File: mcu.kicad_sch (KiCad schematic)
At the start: 43 parts, among them J5 Conn_01x04_Socket, SW1 SW_Push, SW2 SW_Push, U2 ESP32-S3-WROOM-1, U3 SN74AXC4T245PWR, Y1 32.768kHz

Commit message: Schematic + Layout Review Ready First Rev
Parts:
- TP1, TP10, TP11, TP2, TP3, TP4, TP5, TP6, TP7, TP8, TP9: footprint (none) -> TestPoint:TestPoint_THTPad_1.5x1.5mm_Drill0.7mm
- U3: footprint SN74AXC4T245PWR:SOP65P640X120-16N -> footprints:SOP65P640X120-16N
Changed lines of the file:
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@@
 			)
 		)
-		(property "Footprint" ""
+		(property "Footprint" "TestPoint:TestPoint_THTPad_1.5x1.5mm_Drill0.7mm"
 			(at 227.33 123.19 0)
 			(effects
@@
 			)
 		)
-		(property "Footprint" ""
+		(property "Footprint" "TestPoint:TestPoint_THTPad_1.5x1.5mm_Drill0.7mm"
 			(at 227.33 133.35 0)
 			(effects
@@
 			)
 		)
-		(property "Footprint" ""
+		(property "Footprint" "TestPoint:TestPoint_THTPad_1.5x1.5mm_Drill0.7mm"
 			(at 222.25 106.68 0)
 			(effects
@@
 			)
 		)
-		(property "Footprint" ""
+		(property "Footprint" "TestPoint:TestPoint_THTPad_1.5x1.5mm_Drill0.7mm"
 			(at 256.54 133.35 0)
 			(effects
@@
 			)
 		)
-		(property "Footprint" ""
+		(property "Footprint" "TestPoint:TestPoint_THTPad_1.5x1.5mm_Drill0.7mm"
 			(at 256.54 118.11 0)
 			(effects
@@
 			)
 		)
-		(property "Footprint" ""
+		(property "Footprint" "TestPoint:TestPoint_THTPad_1.5x1.5mm_Drill0.7mm"
 			(at 260.35 106.68 0)
 			(effects
@@
 			)
 		)
-		(property "Footprint" ""
+		(property "Footprint" "TestPoint:TestPoint_THTPad_1.5x1.5mm_Drill0.7mm"
 			(at 256.54 128.27 0)
 			(effects
@@
 			)
 		)
-		(property "Footprint" "SN74AXC4T245PWR:SOP65P640X120-16N"
+		(property "Footprint" "footprints:SOP65P640X120-16N"
 			(at 166.37 110.49 0)
 			(effects
@@
 			)
 		)
-		(property "Footprint" ""
+		(property "Footprint" "TestPoint:TestPoint_THTPad_1.5x1.5mm_Drill0.7mm"
 			(at 256.54 123.19 0)
 			(effects
@@
 			)
 		)
-		(property "Footprint" ""
+		(property "Footprint" "TestPoint:TestPoint_THTPad_1.5x1.5mm_Drill0.7mm"
 			(at 241.3 106.68 0)
 			(effects
@@
 			)
 		)
-		(property "Footprint" ""
+		(property "Footprint" "TestPoint:TestPoint_THTPad_1.5x1.5mm_Drill0.7mm"
 			(at 227.33 118.11 0)
 			(effects
@@
 			)
 		)
-		(property "Footprint" ""
+		(property "Footprint" "TestPoint:TestPoint_THTPad_1.5x1.5mm_Drill0.7mm"
 			(at 227.33 128.27 0)
 			(effects

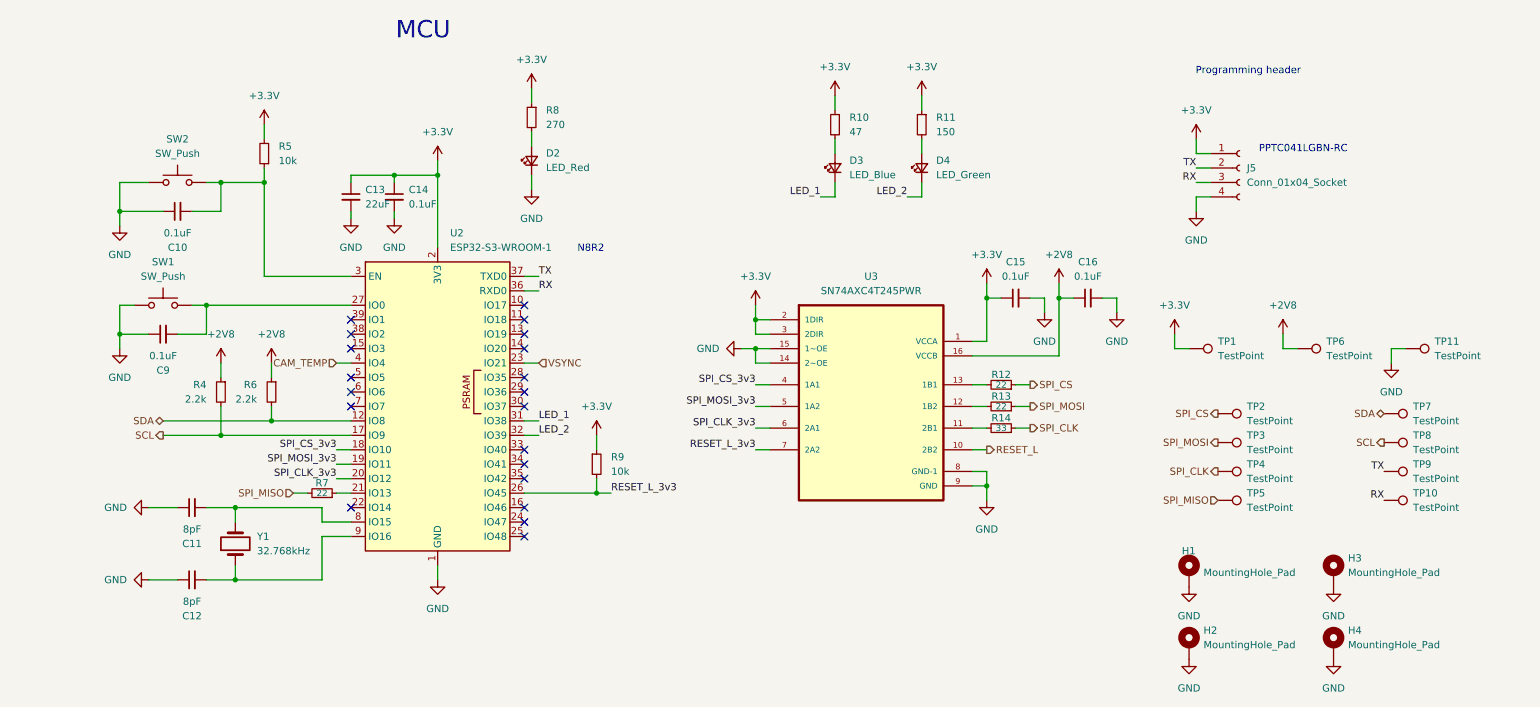
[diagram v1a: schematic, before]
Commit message: rev 2 added usb prog and i2c level shifting
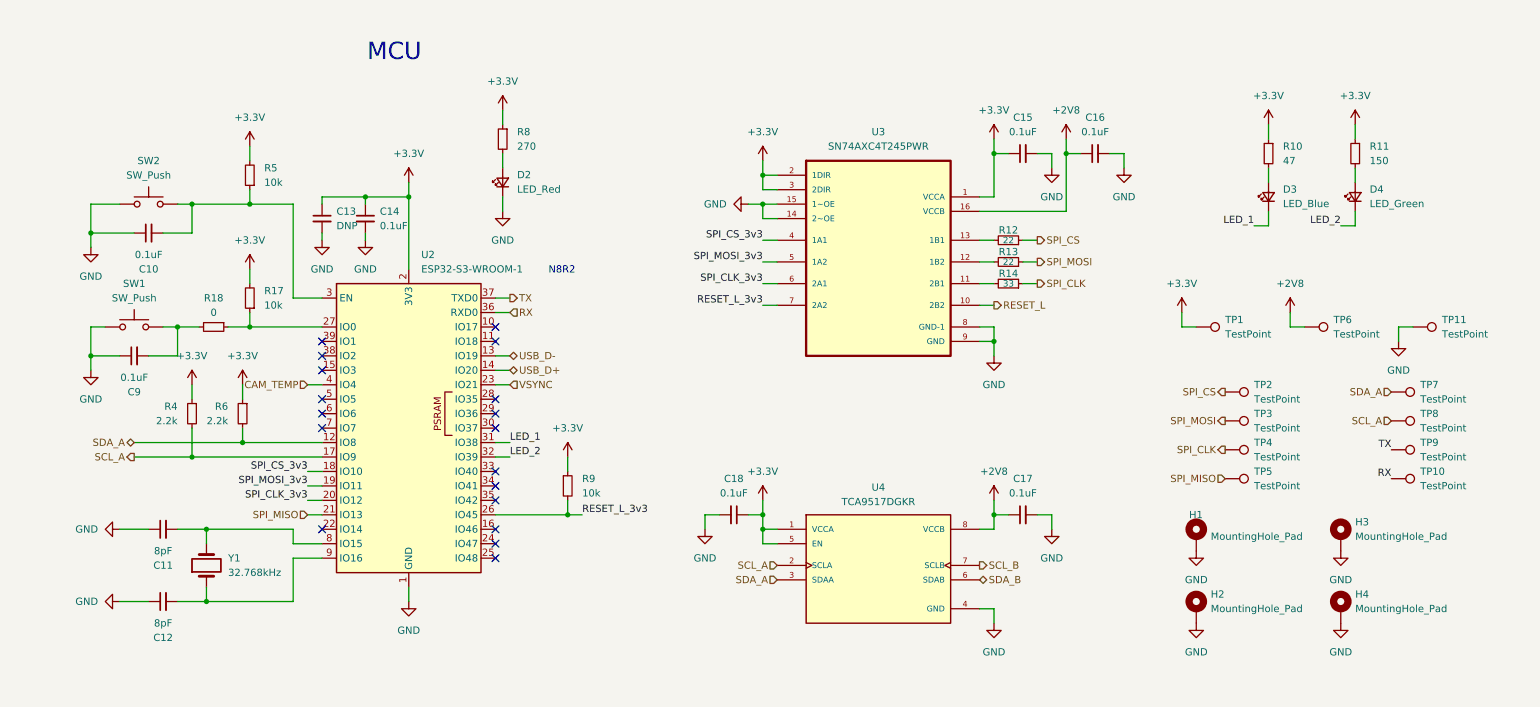
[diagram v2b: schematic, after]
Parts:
- removed J5: Conn_01x04_Socket, Connector_PinSocket_2.54mm:PinSocket_1x04_P2.54mm_Vertical, symbol Connector:Conn_01x04_Socket
- removed R7: 22, Resistor_SMD:R_0805_2012Metric_Pad1.20x1.40mm_HandSolder, symbol Device:R_Small
- added C17, C18: 0.1uF, Capacitor_SMD:C_0805_2012Metric_Pad1.18x1.45mm_HandSolder, symbol Device:C_Small
- added R17: 10k, Resistor_SMD:R_0805_2012Metric_Pad1.20x1.40mm_HandSolder, symbol Device:R_Small
- added R18: 0, Resistor_SMD:R_0805_2012Metric_Pad1.20x1.40mm_HandSolder, symbol Device:R_Small
- added U4: TCA9517DGKR, footprints:SOP65P490X110-8N, symbol TCA9517DGKR:TCA9517DGKR
- C13: value 22uF -> DNP
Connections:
- net +2V8: now also C17.1, U4.8 (VCCB); no longer R4.1, R6.1
- net +3.3V: now also R4.1, R6.1, C18.1, R17.2, U4.1 (VCCA), U4.5 (EN)
- net GND: now also C17.2, C18.2, U4.4 (GND)
- net SPI_MISO: now also U2.21 (IO13)
- net USB_D-: now reaches U2.13 (IO19)
- net USB_D+: now reaches U2.14 (IO20)
- net at C9.2, SW1.2: now also R18.2; no longer U2.27 (IO0)
- net SCL renamed SCL_A
- net SCL_A: now also U4.2 (SCLA)
- net SDA renamed SDA_A
- net SDA_A: now also U4.3 (SDAA)
- new net: R17.1, R18.1, U2.27 (IO0)
- new net SCL_B: U4.7 (SCLB)
- new net SDA_B: U4.6 (SDAB)
- no-connect marks 20 -> 18
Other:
- note removed: "PPTC041LGBN-RC"
- note removed: "Programming header"
- moved on the sheet: C10, C11, C12, C13, C14, C15, C16, C9, D2, D3, D4, H1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

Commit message: Updated Schematic and fixed some routing issues
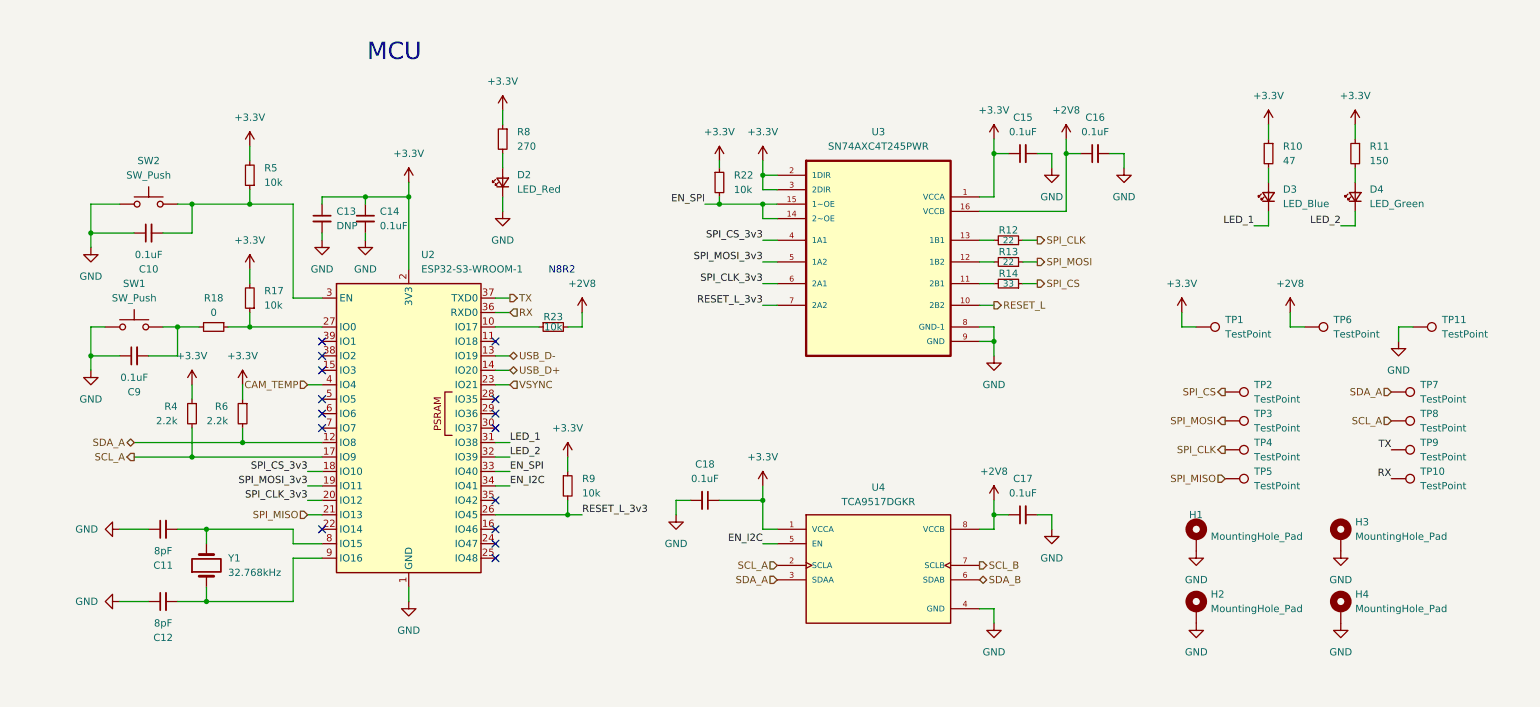
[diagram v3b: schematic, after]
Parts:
- added R22, R23: 10k, Resistor_SMD:R_0805_2012Metric_Pad1.20x1.40mm_HandSolder, symbol Device:R_Small
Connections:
- net +2V8: now also R23.2
- net +3.3V: now also R22.1; no longer U4.5 (EN)
- net GND: no longer U3.14 (2~OE), U3.15 (1~OE)
- net SPI_CLK: now also R12.1; no longer R14.1
- net SPI_CS: now also R14.1; no longer R12.1
- net at U2.10 (IO17): now also R23.1
- net EN_SPI: now reaches U2.33 (IO40)
- net EN_SPI: now also U3.14 (2~OE), U3.15 (1~OE), R22.2
- net EN_I2C: now reaches U2.34 (IO41)
- net EN_I2C: now also U4.5 (EN)
- no-connect marks 18 -> 15
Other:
- moved on the sheet: C18

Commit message: Rev A PCB Ordered
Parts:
- removed TP11: TestPoint, TestPoint:TestPoint_THTPad_1.5x1.5mm_Drill0.7mm, symbol Connector:TestPoint
- added C19: 1uF, Capacitor_SMD:C_0805_2012Metric_Pad1.18x1.45mm_HandSolder, symbol Device:C_Small
- added R20, R21: 2.2k, Resistor_SMD:R_0805_2012Metric_Pad1.20x1.40mm_HandSolder, symbol Device:R_Small
- added R25, R28: 10k, Resistor_SMD:R_0805_2012Metric_Pad1.20x1.40mm_HandSolder, symbol Device:R_Small
- added R26, R27: 47k, Resistor_SMD:R_0805_2012Metric_Pad1.20x1.40mm_HandSolder, symbol Device:R_Small
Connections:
- net +2V8: now also C18.2, U4.1 (VCCA), C19.2, R20.1, R21.1, R25.1, R26.1, R28.2; no longer C17.1, U4.8 (VCCB)
- net +3.3V: now also C17.1, U4.8 (VCCB); no longer C18.1, U4.1 (VCCA)
- net GND: now also C18.1, C19.1, R27.2; no longer C18.2
- net RESET_L: now also R28.1
- net SCL_A: now also U4.7 (SCLB); no longer U4.2 (SCLA)
- net SCL_B: now also U4.2 (SCLA), R20.2; no longer U4.7 (SCLB)
- net SDA_A: now also U4.6 (SDAB); no longer U4.3 (SDAA)
- net SDA_B: now also U4.3 (SDAA), R21.2; no longer U4.6 (SDAB)
- net SPI_CLK: now also R26.2
- net SPI_CS: now also R25.2
- net SPI_MOSI: now also R27.1
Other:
- note added: "Detect 2.8V Present"
- note added: "EN Internal Pullup to VCCB"
- note added: "LEDs"
- note added: "Level Shifters"
- note added: "Mounting Holes"
- note added: "TPs"
- company: (none) -> FrostByte Solutions
- title: (none) -> FrostByte IR Camera Interface Board
- moved on the sheet: C10, C11, C12, C13, C14, C15, C16, C17, C18, C9, D2, D3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
